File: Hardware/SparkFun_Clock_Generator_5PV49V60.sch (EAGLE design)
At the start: 37 parts, among them U1 IDT_5P49V60_CLOCK_GENERATOR, Y1 16MHz

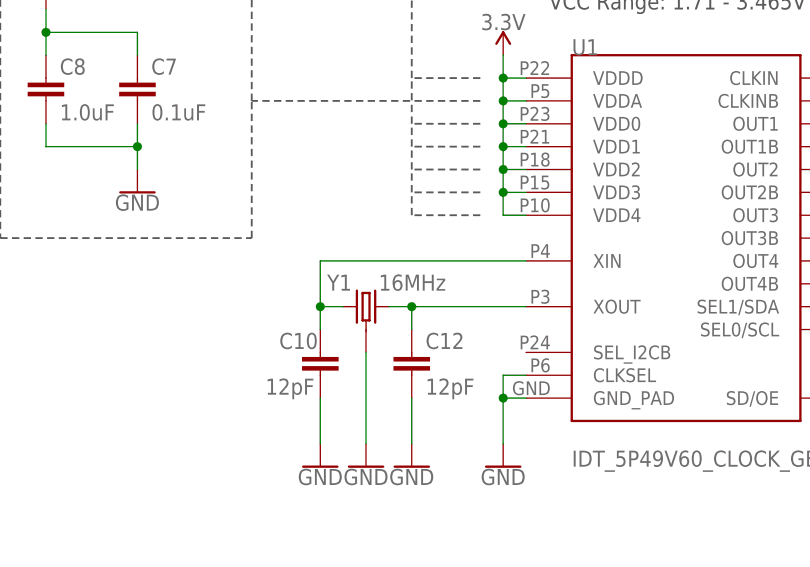
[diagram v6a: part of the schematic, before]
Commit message: Updates crystal and 12pF parts
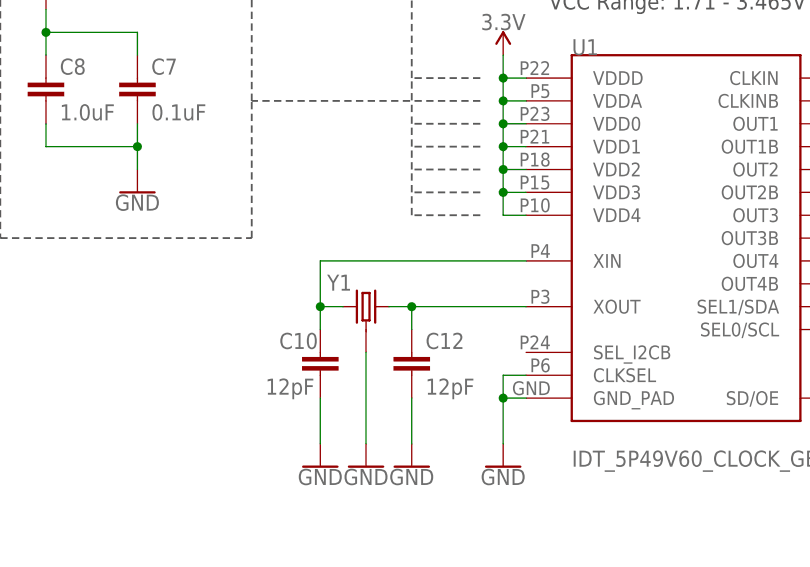
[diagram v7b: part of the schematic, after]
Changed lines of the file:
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@@
 </instance>
 <instance part="Y1" gate="G$1" x="55.88" y="73.66" smashed="yes" rot="MR0">
-<attribute name="VALUE" x="64.77" y="77.216" size="1.778" layer="96" font="vector" rot="MR0" align="top-left"/>
 <attribute name="NAME" x="51.562" y="77.216" size="1.778" layer="95" font="vector" rot="MR0" align="top-right"/>
 </instance>

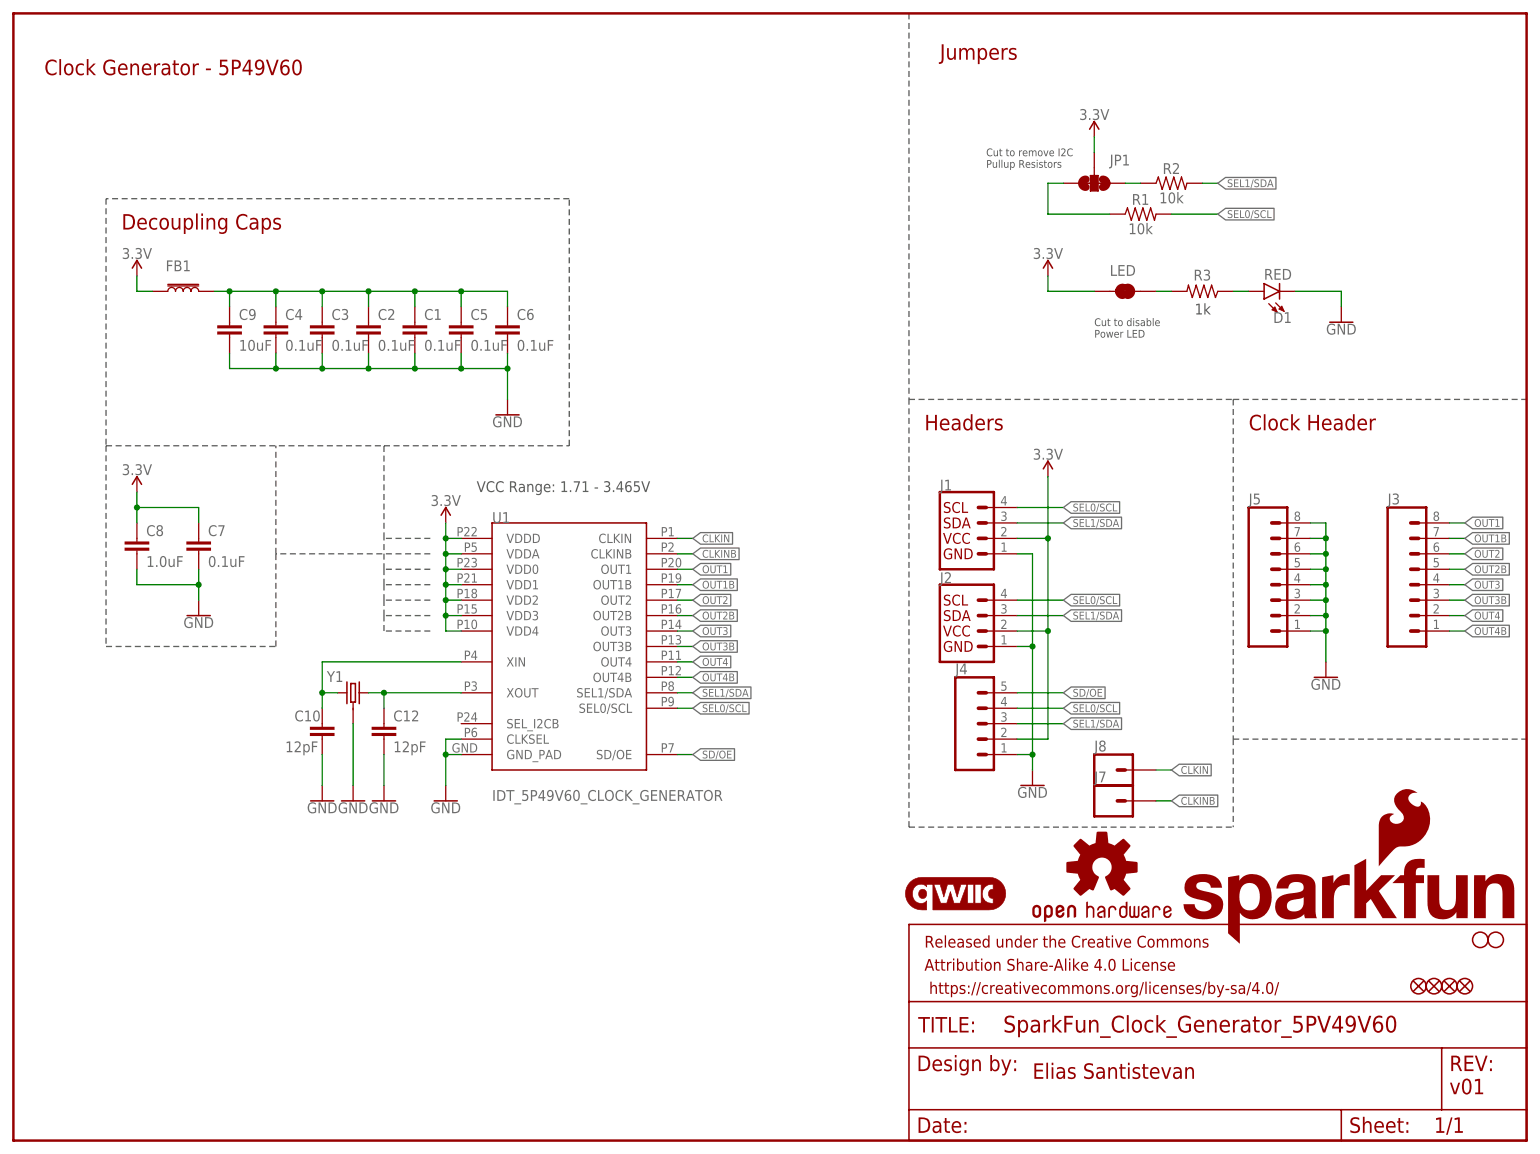
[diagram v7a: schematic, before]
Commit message: Adds default address to schematic, moves design to 0,0 , updates right angle qwiic connector with value
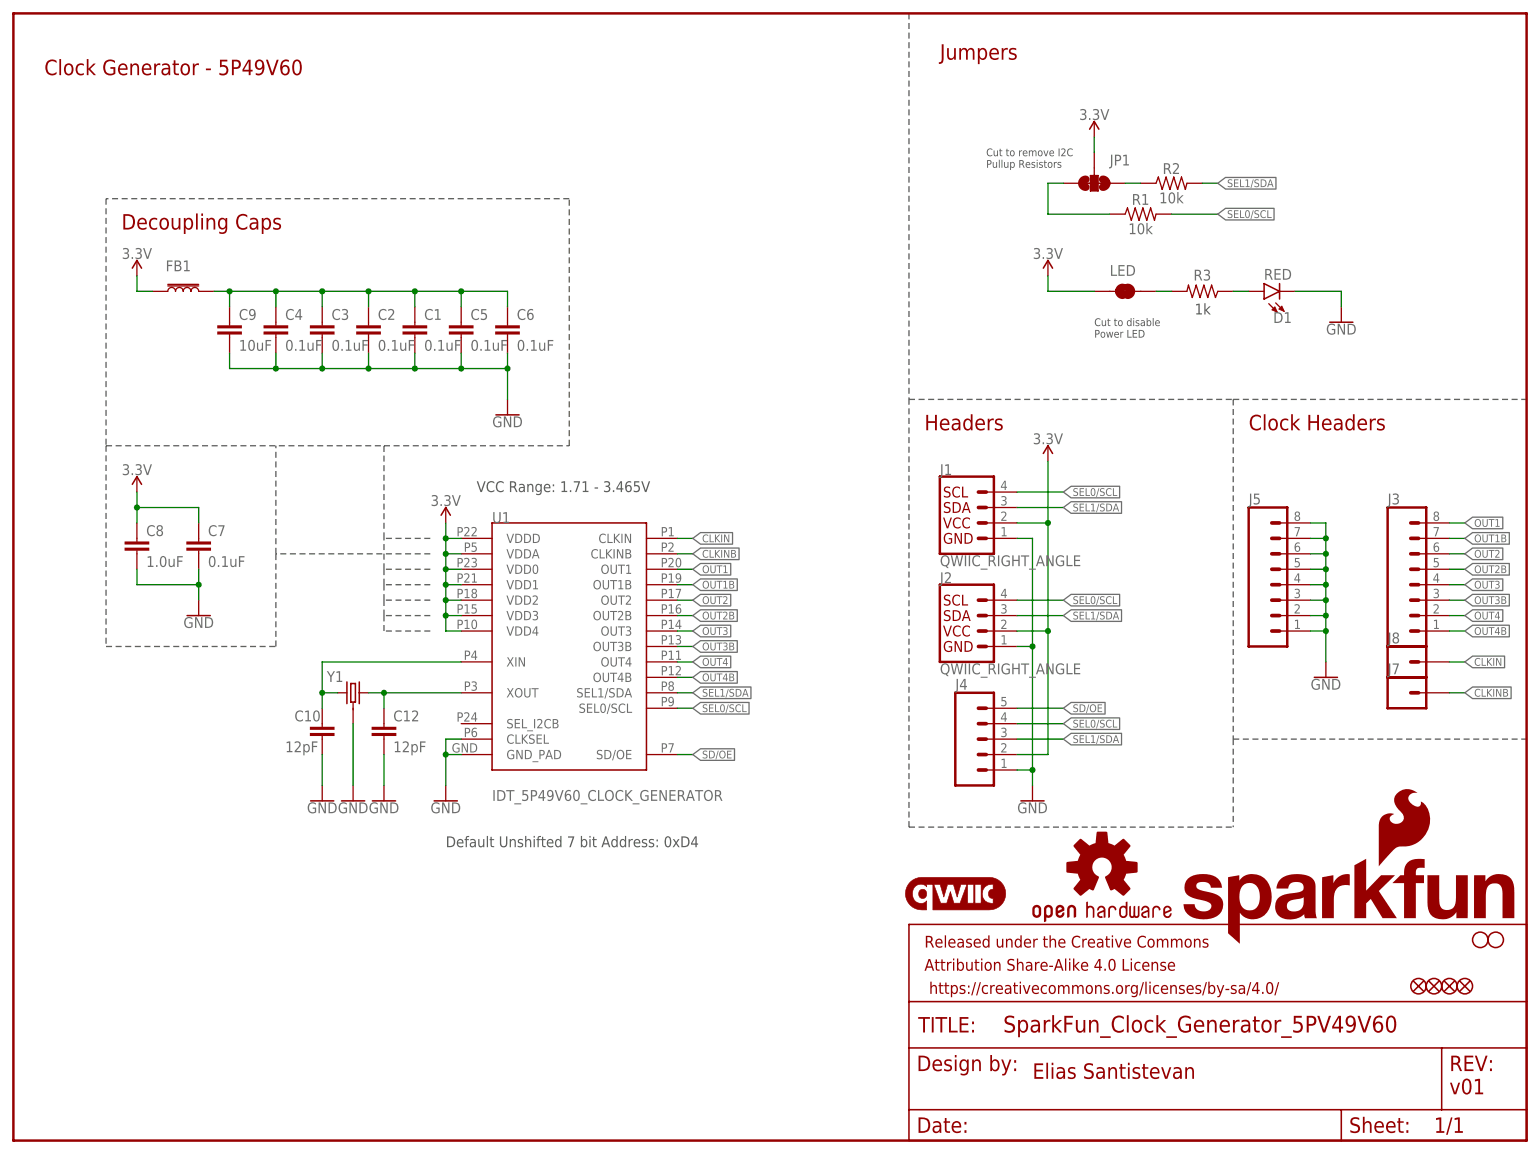
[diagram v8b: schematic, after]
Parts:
- J1, J2: value (none) -> QWIIC_RIGHT_ANGLE
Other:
- note added: "Clock Headers"
- note added: "Default Unshifted 7 bit Address: 0xD4"
- note removed: "Clock Header"
- moved on the sheet: J1, J4, J7, J8
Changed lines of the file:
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@@
 <parts>
 <part name="FRAME1" library="SparkFun-Aesthetics" deviceset="FRAME-LETTER" device=""/>
-<part name="J1" library="SparkFun-Connectors" deviceset="QWIIC_CONNECTOR" device="JS-1MM"/>
-<part name="J2" library="SparkFun-Connectors" deviceset="QWIIC_CONNECTOR" device="JS-1MM"/>
+<part name="J1" library="SparkFun-Connectors" deviceset="QWIIC_CONNECTOR" device="JS-1MM" value="QWIIC_RIGHT_ANGLE"/>
+<part name="J2" library="SparkFun-Connectors" deviceset="QWIIC_CONNECTOR" device="JS-1MM" value="QWIIC_RIGHT_ANGLE"/>
 <part name="U1" library="clock" deviceset="IDT_5P49V60_CLOCK_GENERATOR" device=""/>
 <part name="GND1" library="SparkFun-PowerSymbols" deviceset="GND" device=""/>
@@
 <text x="152.4" y="177.8" size="2.54" layer="94" font="vector">Jumpers</text>
 <text x="149.86" y="116.84" size="2.54" layer="94" font="vector">Headers</text>
-<text x="203.2" y="116.84" size="2.54" layer="94" font="vector">Clock Header</text>
+<text x="203.2" y="116.84" size="2.54" layer="94" font="vector">Clock Headers</text>
 <text x="17.78" y="149.86" size="2.54" layer="94" font="vector">Decoupling Caps</text>
 <wire x1="147.32" y1="51.562" x2="147.32" y2="121.92" width="0.2032" layer="97" style="shortdash"/>
@@
 <text x="76.2" y="106.68" size="1.778" layer="97" font="vector">VCC Range: 1.71 - 3.465V</text>
 <text x="194.31" y="135.89" size="1.778" layer="97" font="vector">1k</text>
+<text x="71.12" y="48.26" size="1.778" layer="97" font="vector">Default Unshifted 7 bit Address: 0xD4</text>
 </plain>
 <instances>
@@
 <attribute name="REV" x="236.22" y="6.604" size="2.7432" layer="94" font="vector"/>
 </instance>
-<instance part="J1" gate="G$1" x="157.48" y="99.06" smashed="yes">
-<attribute name="VALUE" x="152.4" y="93.726" size="1.778" layer="96" font="vector" align="top-left"/>
-<attribute name="NAME" x="152.4" y="106.934" size="1.778" layer="95" font="vector"/>
+<instance part="J1" gate="G$1" x="157.48" y="101.6" smashed="yes">
+<attribute name="VALUE" x="152.4" y="96.266" size="1.778" layer="96" font="vector" align="top-left"/>
+<attribute name="NAME" x="152.4" y="109.474" size="1.778" layer="95" font="vector"/>
 </instance>
 <instance part="J2" gate="G$1" x="157.48" y="83.82" smashed="yes">
@@
 <attribute name="VALUE" x="71.12" y="104.394" size="1.778" layer="96" align="bottom-center"/>
 </instance>
-<instance part="SUPPLY2" gate="G$1" x="170.18" y="109.22" smashed="yes">
-<attribute name="VALUE" x="170.18" y="112.014" size="1.778" layer="96" align="bottom-center"/>
-</instance>
-<instance part="GND2" gate="1" x="167.64" y="58.42" smashed="yes">
-<attribute name="VALUE" x="167.64" y="58.166" size="1.778" layer="96" align="top-center"/>
-</instance>
-<instance part="J4" gate="G$1" x="157.48" y="68.58" smashed="yes">
-<attribute name="VALUE" x="154.94" y="58.674" size="1.778" layer="96" font="vector"/>
-<attribute name="NAME" x="154.94" y="76.708" size="1.778" layer="95" font="vector"/>
+<instance part="SUPPLY2" gate="G$1" x="170.18" y="111.76" smashed="yes">
+<attribute name="VALUE" x="170.18" y="114.554" size="1.778" layer="96" align="bottom-center"/>
+</instance>
+<instance part="GND2" gate="1" x="167.64" y="55.88" smashed="yes">
+<attribute name="VALUE" x="167.64" y="55.626" size="1.778" layer="96" align="top-center"/>
+</instance>
+<instance part="J4" gate="G$1" x="157.48" y="66.04" smashed="yes">
+<attribute name="VALUE" x="154.94" y="56.134" size="1.778" layer="96" font="vector"/>
+<attribute name="NAME" x="154.94" y="74.168" size="1.778" layer="95" font="vector"/>
 </instance>
 <instance part="H1" gate="G$1" x="243.84" y="33.02" smashed="yes"/>
@@
 <instance part="LOGO2" gate="G$1" x="179.07" y="44.958" smashed="yes"/>
 <instance part="LOGO3" gate="G$1" x="154.94" y="40.64" smashed="yes"/>
-<instance part="J7" gate="G$1" x="180.34" y="55.88" smashed="yes">
-<attribute name="VALUE" x="177.8" y="51.054" size="1.778" layer="96" font="vector"/>
-<attribute name="NAME" x="177.8" y="58.928" size="1.778" layer="95" font="vector"/>
-</instance>
-<instance part="J8" gate="G$1" x="180.34" y="60.96" smashed="yes">
-<attribute name="VALUE" x="177.8" y="56.134" size="1.778" layer="96" font="vector"/>
-<attribute name="NAME" x="177.8" y="64.008" size="1.778" layer="95" font="vector"/>
+<instance part="J7" gate="G$1" x="228.6" y="73.66" smashed="yes">
+<attribute name="VALUE" x="226.06" y="68.834" size="1.778" layer="96" font="vector"/>
+<attribute name="NAME" x="226.06" y="76.708" size="1.778" layer="95" font="vector"/>
+</instance>
+<instance part="J8" gate="G$1" x="228.6" y="78.74" smashed="yes">
+<attribute name="VALUE" x="226.06" y="73.914" size="1.778" layer="96" font="vector"/>
+<attribute name="NAME" x="226.06" y="81.788" size="1.778" layer="95" font="vector"/>
 </instance>
 <instance part="J3" gate="G$1" x="231.14" y="91.44" smashed="yes">
@@
 <segment>
 <pinref part="GND2" gate="1" pin="GND"/>
-<wire x1="165.1" y1="63.5" x2="167.64" y2="63.5" width="0.1524" layer="91"/>
-<wire x1="167.64" y1="63.5" x2="167.64" y2="60.96" width="0.1524" layer="91"/>
+<wire x1="165.1" y1="60.96" x2="167.64" y2="60.96" width="0.1524" layer="91"/>
+<wire x1="167.64" y1="60.96" x2="167.64" y2="58.42" width="0.1524" layer="91"/>
 <pinref part="J4" gate="G$1" pin="1"/>
 <pinref part="J1" gate="G$1" pin="1"/>
-<wire x1="165.1" y1="96.52" x2="167.64" y2="96.52" width="0.1524" layer="91"/>
-<wire x1="167.64" y1="96.52" x2="167.64" y2="81.28" width="0.1524" layer="91"/>
+<wire x1="165.1" y1="99.06" x2="167.64" y2="99.06" width="0.1524" layer="91"/>
+<wire x1="167.64" y1="99.06" x2="167.64" y2="81.28" width="0.1524" layer="91"/>
 <pinref part="J2" gate="G$1" pin="1"/>
 <wire x1="165.1" y1="81.28" x2="167.64" y2="81.28" width="0.1524" layer="91"/>
-<wire x1="167.64" y1="81.28" x2="167.64" y2="63.5" width="0.1524" layer="91"/>
+<wire x1="167.64" y1="81.28" x2="167.64" y2="60.96" width="0.1524" layer="91"/>
 <junction x="167.64" y="81.28"/>
-<junction x="167.64" y="63.5"/>
+<junction x="167.64" y="60.96"/>
 </segment>
 <segment>
@@
 <segment>
 <pinref part="J1" gate="G$1" pin="2"/>
-<wire x1="165.1" y1="99.06" x2="170.18" y2="99.06" width="0.1524" layer="91"/>
+<wire x1="165.1" y1="101.6" x2="170.18" y2="101.6" width="0.1524" layer="91"/>
 <pinref part="SUPPLY2" gate="G$1" pin="3.3V"/>
-<wire x1="170.18" y1="99.06" x2="170.18" y2="109.22" width="0.1524" layer="91"/>
+<wire x1="170.18" y1="101.6" x2="170.18" y2="111.76" width="0.1524" layer="91"/>
 <pinref part="J2" gate="G$1" pin="2"/>
 <wire x1="165.1" y1="83.82" x2="170.18" y2="83.82" width="0.1524" layer="91"/>
-<wire x1="170.18" y1="83.82" x2="170.18" y2="99.06" width="0.1524" layer="91"/>
-<junction x="170.18" y="99.06"/>
+<wire x1="170.18" y1="83.82" x2="170.18" y2="101.6" width="0.1524" layer="91"/>
+<junction x="170.18" y="101.6"/>
 <pinref part="J4" gate="G$1" pin="2"/>
-<wire x1="165.1" y1="66.04" x2="170.18" y2="66.04" width="0.1524" layer="91"/>
-<wire x1="170.18" y1="66.04" x2="170.18" y2="83.82" width="0.1524" layer="91"/>
+<wire x1="165.1" y1="63.5" x2="170.18" y2="63.5" width="0.1524" layer="91"/>
+<wire x1="170.18" y1="63.5" x2="170.18" y2="83.82" width="0.1524" layer="91"/>
 <junction x="170.18" y="83.82"/>
 </segment>
@@
 <segment>
 <pinref part="J1" gate="G$1" pin="3"/>
-<wire x1="165.1" y1="101.6" x2="172.72" y2="101.6" width="0.1524" layer="91"/>
-<label x="172.72" y="101.6" size="1.27" layer="95" font="vector" xref="yes"/>
+<wire x1="165.1" y1="104.14" x2="172.72" y2="104.14" width="0.1524" layer="91"/>
+<label x="172.72" y="104.14" size="1.27" layer="95" font="vector" xref="yes"/>
 </segment>
 <segment>
@@
 <segment>
 <pinref part="J4" gate="G$1" pin="3"/>
-<wire x1="165.1" y1="68.58" x2="172.72" y2="68.58" width="0.1524" layer="91"/>
-<label x="172.72" y="68.58" size="1.27" layer="95" font="vector" xref="yes"/>
+<wire x1="165.1" y1="66.04" x2="172.72" y2="66.04" width="0.1524" layer="91"/>
+<label x="172.72" y="66.04" size="1.27" layer="95" font="vector" xref="yes"/>
 </segment>
 <segment>
@@
 <segment>
 <pinref part="J1" gate="G$1" pin="4"/>
-<wire x1="165.1" y1="104.14" x2="172.72" y2="104.14" width="0.1524" layer="91"/>
-<label x="172.72" y="104.14" size="1.27" layer="95" font="vector" xref="yes"/>
+<wire x1="165.1" y1="106.68" x2="172.72" y2="106.68" width="0.1524" layer="91"/>
+<label x="172.72" y="106.68" size="1.27" layer="95" font="vector" xref="yes"/>
 </segment>
 <segment>
 <pinref part="J4" gate="G$1" pin="4"/>
-<wire x1="165.1" y1="71.12" x2="172.72" y2="71.12" width="0.1524" layer="91"/>
-<label x="172.72" y="71.12" size="1.27" layer="95" font="vector" xref="yes"/>
+<wire x1="165.1" y1="68.58" x2="172.72" y2="68.58" width="0.1524" layer="91"/>
+<label x="172.72" y="68.58" size="1.27" layer="95" font="vector" xref="yes"/>
 </segment>
 <segment>
@@
 <segment>
 <pinref part="J4" gate="G$1" pin="5"/>
-<wire x1="165.1" y1="73.66" x2="172.72" y2="73.66" width="0.1524" layer="91"/>
-<label x="172.72" y="73.66" size="1.27" layer="95" font="vector" xref="yes"/>
+<wire x1="165.1" y1="71.12" x2="172.72" y2="71.12" width="0.1524" layer="91"/>
+<label x="172.72" y="71.12" size="1.27" layer="95" font="vector" xref="yes"/>
 </segment>
 </net>
@@
 <segment>
 <pinref part="J8" gate="G$1" pin="1"/>
-<wire x1="190.5" y1="60.96" x2="187.96" y2="60.96" width="0.1524" layer="91"/>
-<label x="190.5" y="60.96" size="1.27" layer="95" font="vector" xref="yes"/>
+<wire x1="238.76" y1="78.74" x2="236.22" y2="78.74" width="0.1524" layer="91"/>
+<label x="238.76" y="78.74" size="1.27" layer="95" font="vector" xref="yes"/>
 </segment>
 </net>
@@
 <segment>
 <pinref part="J7" gate="G$1" pin="1"/>
-<wire x1="190.5" y1="55.88" x2="187.96" y2="55.88" width="0.1524" layer="91"/>
-<label x="190.5" y="55.88" size="1.27" layer="95" font="vector" xref="yes"/>
-</segment>
-</net>
+<wire x1="238.76" y1="73.66" x2="236.22" y2="73.66" width="0.1524" layer="91"/>
+<label x="238.76" y="73.66" size="1.27" layer="95" font="vector" xref="yes"/>
+</segment>
+</net>
